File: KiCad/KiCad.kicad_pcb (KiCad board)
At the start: 2 copper layers, 0 parts

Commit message: Routed STM32 & Various Important components
Routed the Crystal as well as the Capacitors
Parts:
- added C1: 22u, Capacitor_SMD:C_0805_2012Metric, F.Cu at (170.2, 99.1)
- added C10: 100n, Capacitor_SMD:C_0402_1005Metric, F.Cu at (122.4, 83.3)
- added C11: 10n, Capacitor_SMD:C_0402_1005Metric, F.Cu at (118.9, 90.5)
- added C12: 1u, Capacitor_SMD:C_0402_1005Metric, F.Cu at (117.3, 94.0)
- added C13: 1u, Capacitor_SMD:C_0402_1005Metric, F.Cu at (117.3, 95.5)
- added C2: 22u, Capacitor_SMD:C_0805_2012Metric, F.Cu at (160.1, 108.3)
- added C3: 10u, Capacitor_SMD:C_0603_1608Metric, F.Cu at (159.9, 114.8)
- added C4: 100n, Capacitor_SMD:C_0402_1005Metric, F.Cu at (124.5, 98.6)
- added C5: 10p, Capacitor_SMD:C_0402_1005Metric, F.Cu at (116.8, 86.3)
- added C6: 100n, Capacitor_SMD:C_0402_1005Metric, F.Cu at (127.5, 95.5)
- added C7: 100n, Capacitor_SMD:C_0402_1005Metric, F.Cu at (131.1, 86.9)
- added C8: 100n, Capacitor_SMD:C_0402_1005Metric, F.Cu at (118.9, 86.4)
- added C9: 10p, Capacitor_SMD:C_0402_1005Metric, F.Cu at (116.8, 89.4)
- added D1: RED, LED_SMD:LED_0603_1608Metric, F.Cu at (153.3, 105.4)
- added FB1: 120R, Inductor_SMD:L_0603_1608Metric, F.Cu at (119.4, 95.0)
- added J1: Conn_01x04_Male, Connector_PinHeader_2.00mm:PinHeader_1x04_P2.00mm_Vertical, F.Cu at (178.5, 88.2)
- added J2: Conn_01x04_Male, Connector_PinHeader_2.00mm:PinHeader_1x04_P2.00mm_Vertical, F.Cu at (170.4, 88.2)
- added J3: Conn_01x04_Male, Connector_PinHeader_2.00mm:PinHeader_1x04_P2.00mm_Vertical, F.Cu at (174.4, 88.2)
- added J4: USB_B_Micro, Connector_USB:USB_Micro-B_Wuerth_629105150521, F.Cu at (162.5, 101.4)
- added R1: 1k5, Resistor_SMD:R_0402_1005Metric, F.Cu at (184.9, 87.2)
- added R2: 1k5, Resistor_SMD:R_0402_1005Metric, F.Cu at (182.0, 89.2)
- added R3: 1k5, Resistor_SMD:R_0402_1005Metric, F.Cu at (177.9, 97.2)
- added R4: 10k, Resistor_SMD:R_0402_1005Metric, F.Cu at (169.4, 101.6)
- added R5: 1k5, Resistor_SMD:R_0402_1005Metric, F.Cu at (182.0, 87.2)
- added SW1: SW_SPDT, Button_Switch_THT:SW_E-Switch_EG1224_SPDT_Angled, F.Cu at (145.2, 89.8)
- added U1: AMS1117-3.3, Package_TO_SOT_SMD:SOT-223-3_TabPin2, F.Cu at (146.3, 108.2)
- added U2: STM32F103C8T6, Package_QFP:LQFP-48_7x7mm_P0.5mm, F.Cu at (125.0, 89.4)
- added Y1: Crystal_GND24, Crystal:Crystal_SMD_3225-4Pin_3.2x2.5mm_HandSoldering, F.Cu at (113.7, 87.4)

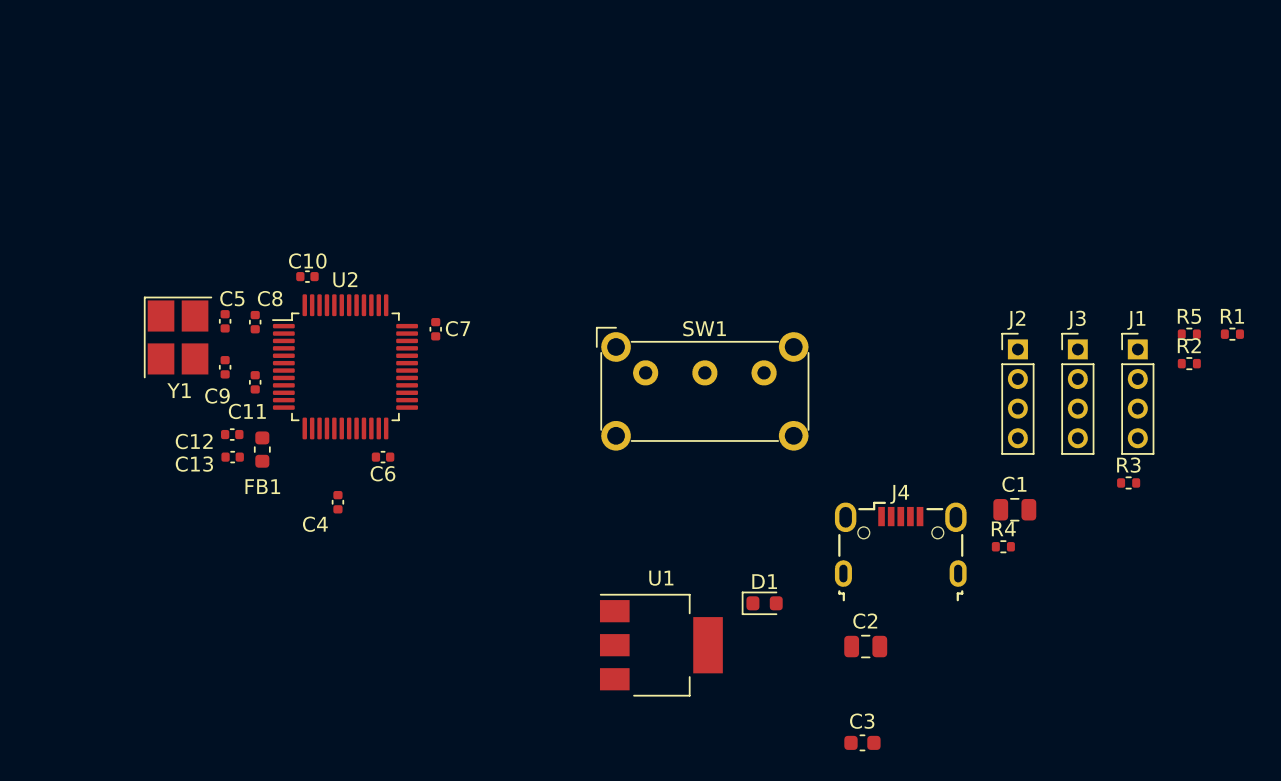
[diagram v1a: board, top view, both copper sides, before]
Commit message: Swapped switch footprint
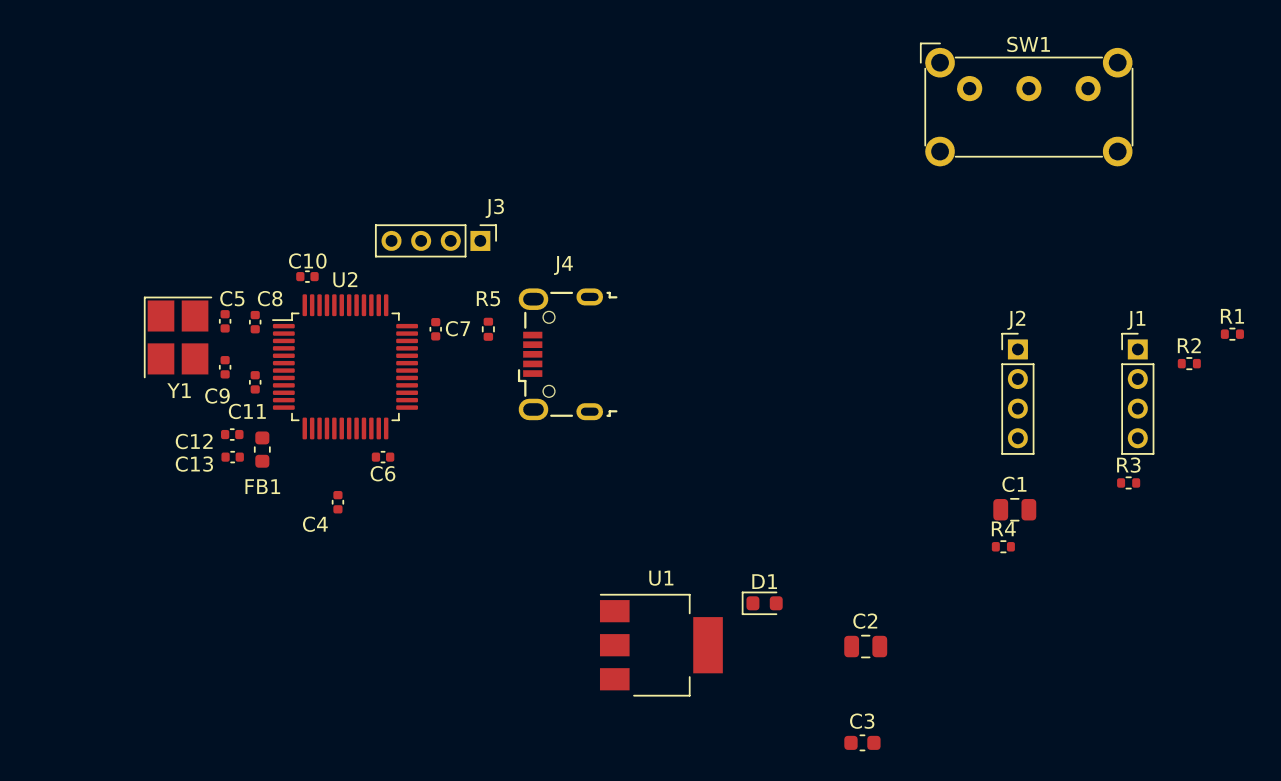
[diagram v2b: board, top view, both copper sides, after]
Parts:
- moved R5 47.4 mm to (134.6, 86.9), turned to 90 degrees
- moved J3 41.0 mm to (134.1, 80.9), turned to -90 degrees
- moved SW1 29.1 mm to (167.1, 70.6)
- moved J4 26.3 mm to (139.5, 88.6), turned to 90 degrees
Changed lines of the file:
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@@
   (net 48 "unconnected-(U2-Pad46)")
   (footprint "Connector_PinHeader_2.00mm:PinHeader_1x04_P2.00mm_Vertical" (layer "F.Cu")
-    (at 174.44 88.23)
+    (at 134.08 80.899 -90)
     (descr "Through hole straight pin header, 1x04, 2.00mm pitch, single row")
     (tags "Through hole pin header THT 1x04 2.00mm single row")
@@
     (property "Sheetname" "")
     (attr through_hole)
-    (fp_text reference "J3" (at 0 -2.06) (layer "F.SilkS")
-      (effects (font (size 1 1) (thickness 0.15)))
-    )
-    (fp_text value "Conn_01x04_Male" (at 0 8.06) (layer "F.Fab")
-      (effects (font (size 1 1) (thickness 0.15)))
-    )
-    (fp_text user "${REFERENCE}" (at 0 3 90) (layer "F.Fab")
+    (fp_text reference "J3" (at -2.286 -1.064 180) (layer "F.SilkS")
+      (effects (font (size 1 1) (thickness 0.15)))
+    )
+    (fp_text value "Conn_01x04_Male" (at 0 8.06 90) (layer "F.Fab")
+      (effects (font (size 1 1) (thickness 0.15)))
+    )
+    (fp_text user "${REFERENCE}" (at 0 3) (layer "F.Fab")
       (effects (font (size 1 1) (thickness 0.15)))
     )
@@
     (fp_line (start -0.5 -1) (end 1 -1) (layer "F.Fab") (width 0.1))
     (fp_line (start -1 7) (end -1 -0.5) (layer "F.Fab") (width 0.1))
-    (pad "1" thru_hole rect (at 0 0) (size 1.35 1.35) (drill 0.8) (layers *.Cu *.Mask)
+    (pad "1" thru_hole rect (at 0 0 270) (size 1.35 1.35) (drill 0.8) (layers *.Cu *.Mask)
       (net 3 "+3.3V") (pinfunction "Pin_1") (pintype "passive"))
-    (pad "2" thru_hole oval (at 0 2) (size 1.35 1.35) (drill 0.8) (layers *.Cu *.Mask)
+    (pad "2" thru_hole oval (at 0 2 270) (size 1.35 1.35) (drill 0.8) (layers *.Cu *.Mask)
       (net 12 "/SWDIO") (pinfunction "Pin_2") (pintype "passive"))
-    (pad "3" thru_hole oval (at 0 4) (size 1.35 1.35) (drill 0.8) (layers *.Cu *.Mask)
+    (pad "3" thru_hole oval (at 0 4 270) (size 1.35 1.35) (drill 0.8) (layers *.Cu *.Mask)
       (net 13 "/SWDCLK") (pinfunction "Pin_3") (pintype "passive"))
-    (pad "4" thru_hole oval (at 0 6) (size 1.35 1.35) (drill 0.8) (layers *.Cu *.Mask)
+    (pad "4" thru_hole oval (at 0 6 270) (size 1.35 1.35) (drill 0.8) (layers *.Cu *.Mask)
       (net 2 "GND") (pinfunction "Pin_4") (pintype "passive"))
     (model "${KICAD6_3DMODEL_DIR}/Connector_PinHeader_2.00mm.3dshapes/PinHeader_1x04_P2.00mm_Vertical.wrl"
@@
   )
   (footprint "Connector_USB:USB_Micro-B_Wuerth_629105150521" (layer "F.Cu")
-    (at 162.48 101.42)
+    (at 139.518 88.561 90)
     (descr "USB Micro-B receptacle, http://www.mouser.com/ds/2/445/629105150521-469306.pdf")
     (tags "usb micro receptacle")
@@
     (property "Sheetname" "")
     (attr smd)
-    (fp_text reference "J4" (at 0 -3.5) (layer "F.SilkS")
-      (effects (font (size 1 1) (thickness 0.15)))
-    )
-    (fp_text value "USB_B_Micro" (at 0 5.6) (layer "F.Fab")
-      (effects (font (size 1 1) (thickness 0.15)))
-    )
-    (fp_text user "PCB Edge" (at 0 3.75) (layer "Dwgs.User")
+    (fp_text reference "J4" (at 6.101 0.247 180) (layer "F.SilkS")
+      (effects (font (size 1 1) (thickness 0.15)))
+    )
+    (fp_text value "USB_B_Micro" (at 0 5.6 90) (layer "F.Fab")
+      (effects (font (size 1 1) (thickness 0.15)))
+    )
+    (fp_text user "PCB Edge" (at 0 3.75 90) (layer "Dwgs.User")
       (effects (font (size 0.5 0.5) (thickness 0.08)))
     )
-    (fp_text user "${REFERENCE}" (at 0 1.05) (layer "F.Fab")
+    (fp_text user "${REFERENCE}" (at 0 1.05 90) (layer "F.Fab")
       (effects (font (size 1 1) (thickness 0.15)))
     )
@@
     (fp_line (start -1.075 -2.95) (end -1.075 -2.725) (layer "F.Fab") (width 0.15))
     (fp_line (start -3.7 3.15) (end -3.7 4.35) (layer "F.Fab") (width 0.15))
-    (pad "" np_thru_hole oval (at -2.5 -0.8) (size 0.8 0.8) (drill 0.8) (layers *.Cu *.Mask))
-    (pad "" np_thru_hole oval (at 2.5 -0.8) (size 0.8 0.8) (drill 0.8) (layers *.Cu *.Mask))
-    (pad "1" smd rect (at -1.3 -1.9) (size 0.45 1.3) (layers "F.Cu" "F.Paste" "F.Mask")
+    (pad "" np_thru_hole oval (at -2.5 -0.8 90) (size 0.8 0.8) (drill 0.8) (layers *.Cu *.Mask))
+    (pad "" np_thru_hole oval (at 2.5 -0.8 90) (size 0.8 0.8) (drill 0.8) (layers *.Cu *.Mask))
+    (pad "1" smd rect (at -1.3 -1.9 90) (size 0.45 1.3) (layers "F.Cu" "F.Paste" "F.Mask")
       (net 1 "VBUS") (pinfunction "VBUS") (pintype "power_out"))
-    (pad "2" smd rect (at -0.65 -1.9) (size 0.45 1.3) (layers "F.Cu" "F.Paste" "F.Mask")
+    (pad "2" smd rect (at -0.65 -1.9 90) (size 0.45 1.3) (layers "F.Cu" "F.Paste" "F.Mask")
       (net 14 "/USB_D-") (pinfunction "D-") (pintype "bidirectional"))
-    (pad "3" smd rect (at 0 -1.9) (size 0.45 1.3) (layers "F.Cu" "F.Paste" "F.Mask")
+    (pad "3" smd rect (at 0 -1.9 90) (size 0.45 1.3) (layers "F.Cu" "F.Paste" "F.Mask")
       (net 15 "/USB_D+") (pinfunction "D+") (pintype "bidirectional"))
-    (pad "4" smd rect (at 0.65 -1.9) (size 0.45 1.3) (layers "F.Cu" "F.Paste" "F.Mask")
+    (pad "4" smd rect (at 0.65 -1.9 90) (size 0.45 1.3) (layers "F.Cu" "F.Paste" "F.Mask")
       (net 16 "unconnected-(J4-Pad4)") (pinfunction "ID") (pintype "passive+no_connect"))
-    (pad "5" smd rect (at 1.3 -1.9) (size 0.45 1.3) (layers "F.Cu" "F.Paste" "F.Mask")
+    (pad "5" smd rect (at 1.3 -1.9 90) (size 0.45 1.3) (layers "F.Cu" "F.Paste" "F.Mask")
       (net 2 "GND") (pinfunction "GND") (pintype "power_out"))
-    (pad "6" thru_hole oval (at 3.875 1.95) (size 1.15 1.8) (drill oval 0.55 1.2) (layers *.Cu *.Mask)
+    (pad "6" thru_hole oval (at 3.875 1.95 90) (size 1.15 1.8) (drill oval 0.55 1.2) (layers *.Cu *.Mask)
       (net 17 "unconnected-(J4-Pad6)") (pinfunction "Shield") (pintype "passive+no_connect"))
-    (pad "6" thru_hole oval (at 3.725 -1.85) (size 1.45 2) (drill oval 0.85 1.4) (layers *.Cu *.Mask)
+    (pad "6" thru_hole oval (at 3.725 -1.85 90) (size 1.45 2) (drill oval 0.85 1.4) (layers *.Cu *.Mask)
       (net 17 "unconnected-(J4-Pad6)") (pinfunction "Shield") (pintype "passive+no_connect"))
-    (pad "6" thru_hole oval (at -3.875 1.95) (size 1.15 1.8) (drill oval 0.55 1.2) (layers *.Cu *.Mask)
+    (pad "6" thru_hole oval (at -3.875 1.95 90) (size 1.15 1.8) (drill oval 0.55 1.2) (layers *.Cu *.Mask)
       (net 17 "unconnected-(J4-Pad6)") (pinfunction "Shield") (pintype "passive+no_connect"))
-    (pad "6" thru_hole oval (at -3.725 -1.85) (size 1.45 2) (drill oval 0.85 1.4) (layers *.Cu *.Mask)
+    (pad "6" thru_hole oval (at -3.725 -1.85 90) (size 1.45 2) (drill oval 0.85 1.4) (layers *.Cu *.Mask)
       (net 17 "unconnected-(J4-Pad6)") (pinfunction "Shield") (pintype "passive+no_connect"))
     (model "${KICAD6_3DMODEL_DIR}/Connector_USB.3dshapes/USB_Micro-B_Wuerth_629105150521.wrl"
@@
   )
   (footprint "Resistor_SMD:R_0402_1005Metric" (layer "F.Cu")
-    (at 181.97 87.2)
+    (at 134.62 86.87 90)
     (descr "Resistor SMD 0402 (1005 Metric), square (rectangular) end terminal, IPC_7351 nominal, (Body size source: IPC-SM-782 page 72, https://www.pcb-3d.com/wordpress/wp-content/uploads/ipc-sm-782a_amendment_1_and_2.pdf), generated with kicad-footprint-generator")
     (tags "resistor")
@@
     (property "Sheetname" "")
     (attr smd)
-    (fp_text reference "R5" (at 0 -1.17) (layer "F.SilkS")
-      (effects (font (size 1 1) (thickness 0.15)))
-    )
-    (fp_text value "1k5" (at 0 1.17) (layer "F.Fab")
-      (effects (font (size 1 1) (thickness 0.15)))
-    )
-    (fp_text user "${REFERENCE}" (at 0 0) (layer "F.Fab")
+    (fp_text reference "R5" (at 2.034 0 180) (layer "F.SilkS")
+      (effects (font (size 1 1) (thickness 0.15)))
+    )
+    (fp_text value "1k5" (at 0 1.17 90) (layer "F.Fab")
+      (effects (font (size 1 1) (thickness 0.15)))
+    )
+    (fp_text user "${REFERENCE}" (at 0 0 90) (layer "F.Fab")
       (effects (font (size 0.26 0.26) (thickness 0.04)))
     )
@@
     (fp_line (start 0.525 0.27) (end -0.525 0.27) (layer "F.Fab") (width 0.1))
     (fp_line (start -0.525 -0.27) (end 0.525 -0.27) (layer "F.Fab") (width 0.1))
-    (pad "1" smd roundrect (at -0.51 0) (size 0.54 0.64) (layers "F.Cu" "F.Paste" "F.Mask") (roundrect_rratio 0.25)
+    (pad "1" smd roundrect (at -0.51 0 90) (size 0.54 0.64) (layers "F.Cu" "F.Paste" "F.Mask") (roundrect_rratio 0.25)
       (net 15 "/USB_D+") (pintype "passive"))
-    (pad "2" smd roundrect (at 0.51 0) (size 0.54 0.64) (layers "F.Cu" "F.Paste" "F.Mask") (roundrect_rratio 0.25)
+    (pad "2" smd roundrect (at 0.51 0 90) (size 0.54 0.64) (layers "F.Cu" "F.Paste" "F.Mask") (roundrect_rratio 0.25)
       (net 3 "+3.3V") (pintype "passive"))
     (model "${KICAD6_3DMODEL_DIR}/Resistor_SMD.3dshapes/R_0402_1005Metric.wrl"
@@
   )
   (footprint "Button_Switch_THT:SW_E-Switch_EG1224_SPDT_Angled" (layer "F.Cu")
-    (at 145.245 89.815)
+    (at 167.132 70.612)
     (descr "E-Switch slide switch, EG series, SPDT, right angle, http://spec_sheets.e-switch.com/specs/P040042.pdf")
     (tags "switch SPDT")

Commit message: Fixed route line bugs & routed pheriphials
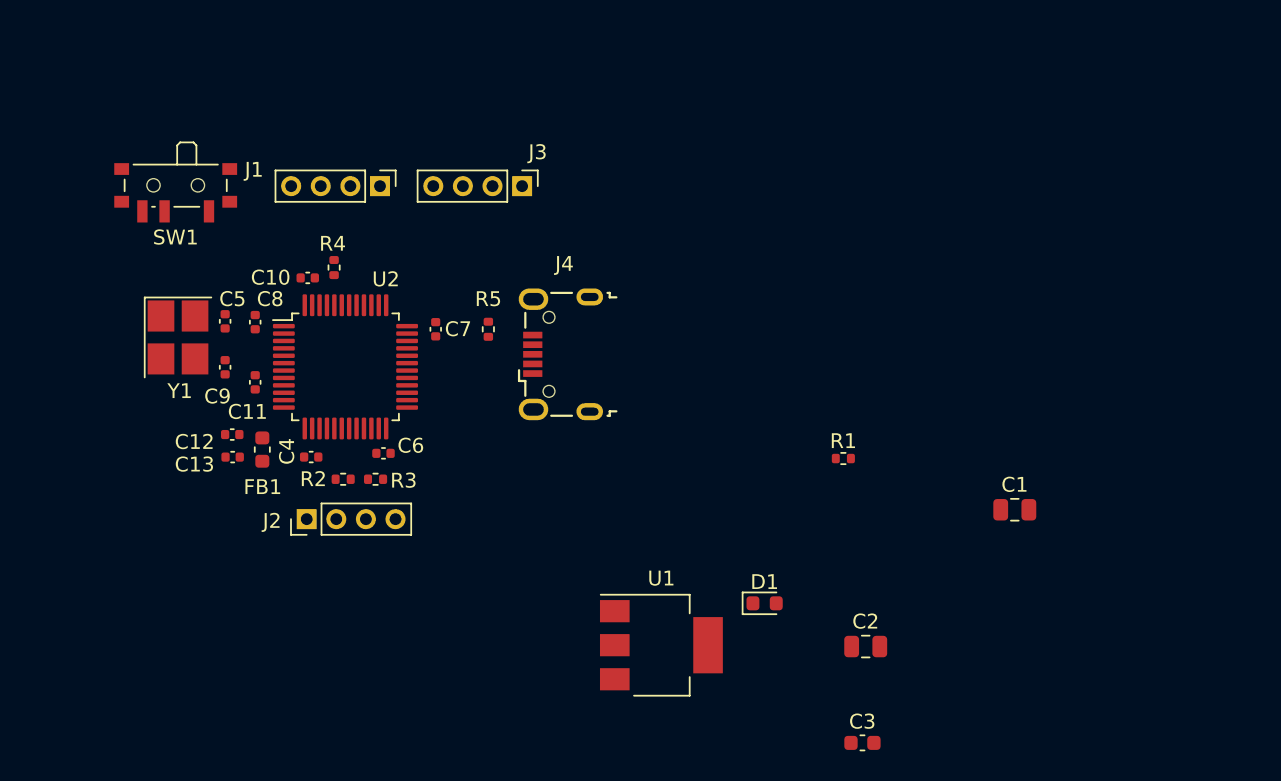
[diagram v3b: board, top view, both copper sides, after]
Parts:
- SW1: footprint Button_Switch_THT:SW_E-Switch_EG1224_SPDT_Angled -> Button_Switch_SMD:SW_SPDT_PCM12
- moved R2 57.7 mm to (124.8, 97.0), turned to 180 degrees
- moved SW1 54.1 mm to (113.5, 77.5), turned to 180 degrees
- moved J1 52.4 mm to (127.3, 77.2), turned to -90 degrees
- moved R3 50.9 mm to (127.0, 97.0)
- moved J2 49.4 mm to (122.3, 99.7), turned to 90 degrees
- moved R4 49.0 mm to (124.2, 82.7), turned to -90 degrees
- moved R1 27.6 mm to (158.6, 95.6)
- moved J3 4.65 mm to (136.9, 77.2)
- moved C4 3.55 mm to (122.7, 95.5), turned to 0 degrees
- moved C6 0.26 mm to (127.5, 95.2)
- moved C10 0.09 mm to (122.4, 83.4)
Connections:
- J1 pad 3: /USART1_TX -> /USART1_RX
- R4 pad 1: /BOOT0 -> /FW_BOOT0
- SW1 pad 1: unconnected-(SW1-Pad1) -> +3.3V
- SW1 pad 2: unconnected-(SW1-Pad2) -> /FW_BOOT0
- SW1 pad 3: unconnected-(SW1-Pad3) -> GND
- U2 pad 43: /USART1_TX -> /USART1_RX
